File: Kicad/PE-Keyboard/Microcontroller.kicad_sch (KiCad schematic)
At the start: 34 parts, among them J1 USB_B_Micro, J2 Conn_01x02, J3 Conn_02x18_Odd_Even, J4 Conn_02x18_Odd_Even, U1 NCP1117-3.3_SOT223, U2 W25Q128JVS, U3 RP2040, Y1 ABLS-12.000MHZ-B4-T

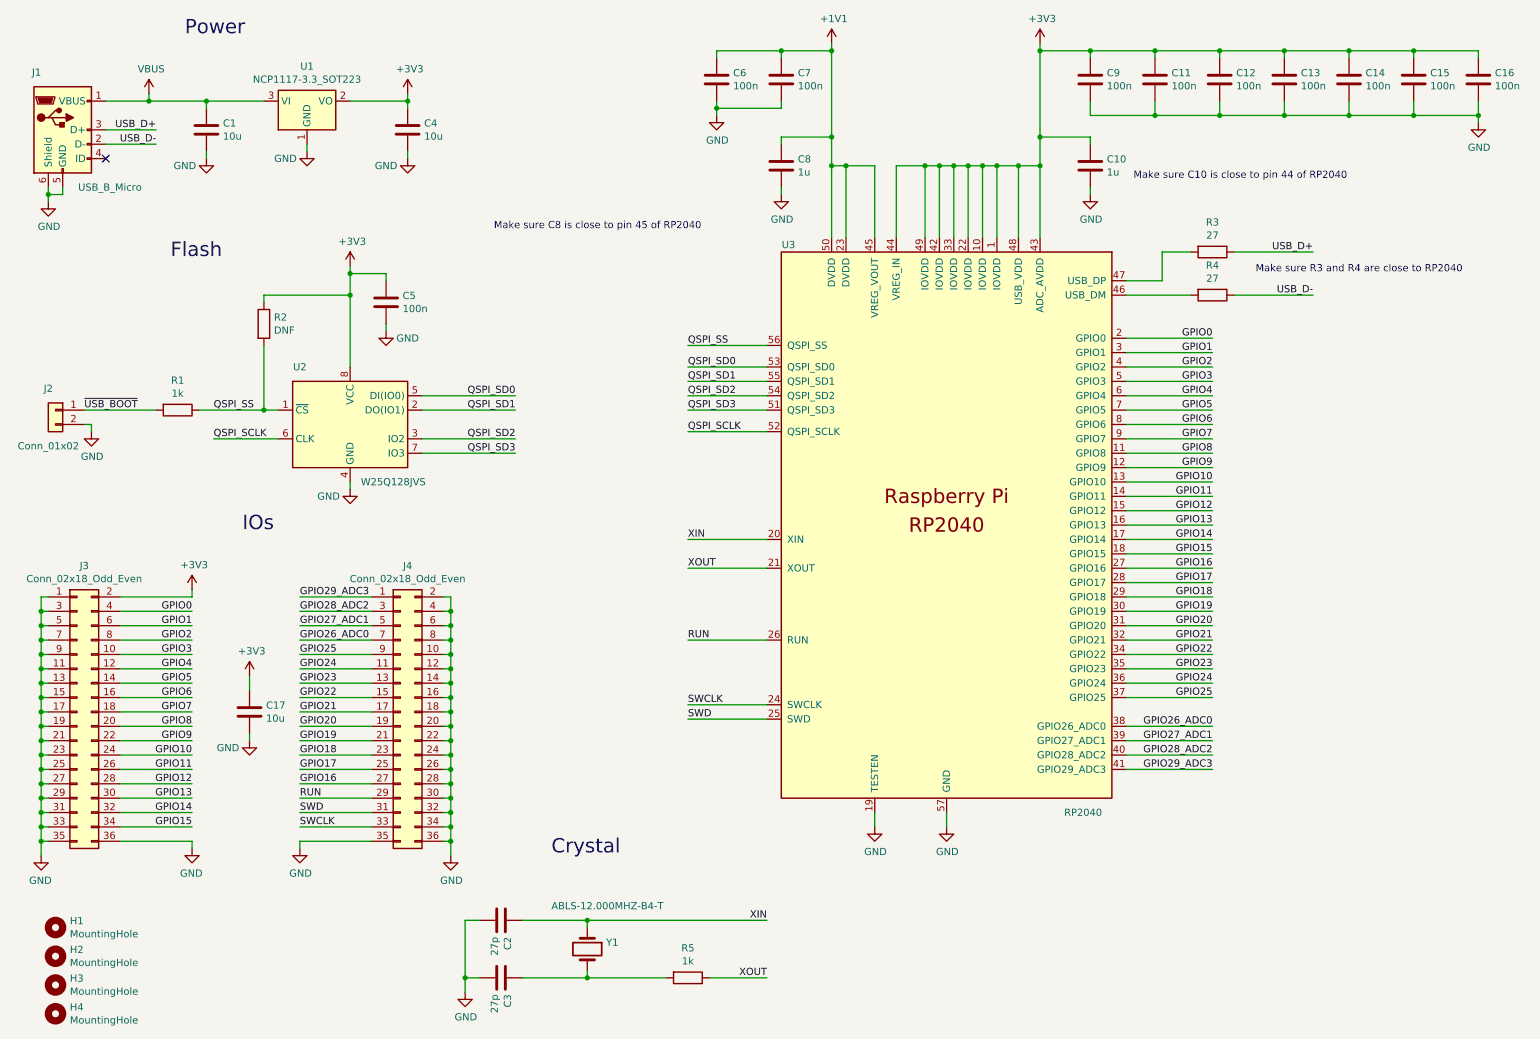
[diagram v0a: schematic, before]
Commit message: Started Sch and PCB
Laid out the buttons/Encoder. Chose a nice crystal, realized a connector in board gives challenges with routing.
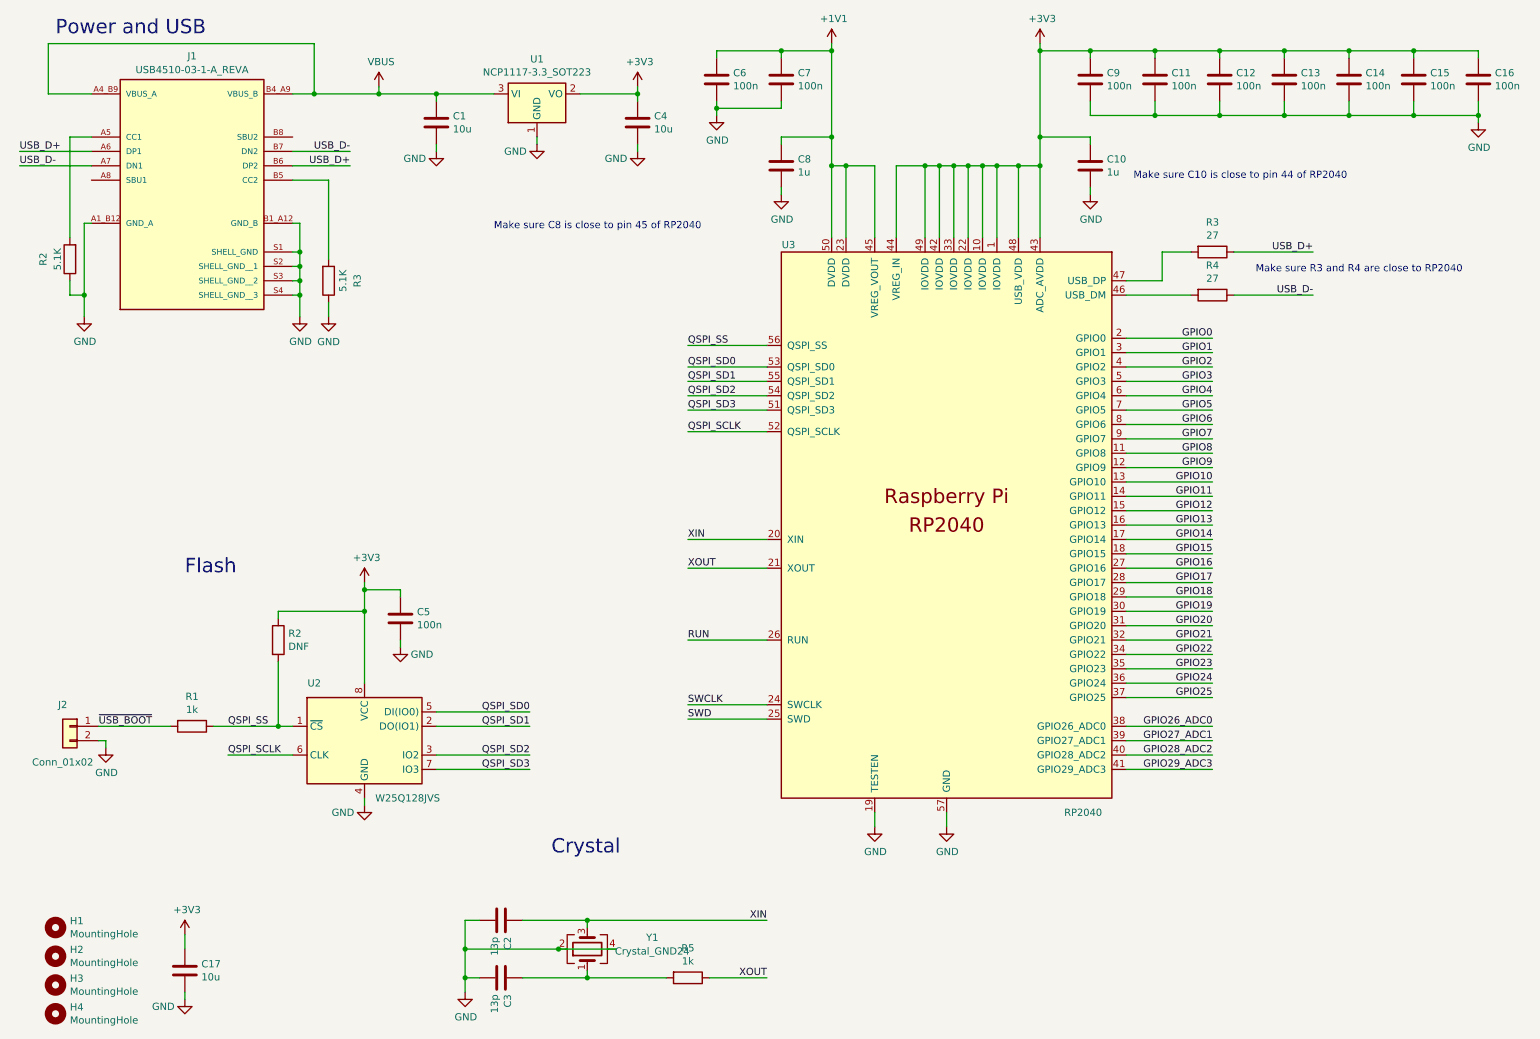
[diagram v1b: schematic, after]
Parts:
- removed J1: USB_B_Micro, RP2040:USB_Micro-B_Amphenol_10103594-0001LF_Horizontal_modified, symbol RP2040_minimal-rescue:USB_B_Micro-Connector
- removed J3, J4: Conn_02x18_Odd_Even, Connector_PinHeader_2.54mm:PinHeader_2x18_P2.54mm_Vertical, symbol Connector_Generic:Conn_02x18_Odd_Even
- removed Y1: ABLS-12.000MHZ-B4-T, RP2040:Crystal_SMD_HC49-US, symbol Device:Crystal
- added J1: USB4510-03-1-A_REVA, PE-Keyboard:GCT_USB4510-03-1-A_REVA, symbol USB4510-03-1-A_REVA:USB4510-03-1-A_REVA
- added R2, R3: 5.1K, Resistor_SMD:R_0603_1608Metric_Pad0.98x0.95mm_HandSolder, symbol Device:R
- added Y1: Crystal_GND24, Crystal:Crystal_SMD_0603-4Pin_6.0x3.5mm_HandSoldering, symbol Device:Crystal_GND24
- C10, C11, C12, C13, C14, C15, C16, C5, C6, C7, C8, C9: footprint Capacitor_SMD:C_0402_1005Metric -> Capacitor_SMD:C_0603_1608Metric_Pad1.08x0.95mm_HandSolder
- C2, C3: value 27p -> 13p; footprint Capacitor_SMD:C_0402_1005Metric -> Capacitor_SMD:C_0603_1608Metric_Pad1.08x0.95mm_HandSolder
- R1, R2, R3, R4, R5: footprint Capacitor_SMD:C_0402_1005Metric -> Resistor_SMD:R_0603_1608Metric_Pad0.98x0.95mm_HandSolder
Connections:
- net GND: now also J1.A1_B12 (GND_A), J1.B1_A12 (GND_B), J1.S1 (SHELL_GND), J1.S2 (SHELL_GND__1), J1.S3 (SHELL_GND__2), J1.S4 (SHELL_GND__3), R2.1, R3.1, Y1.2, Y1.4
- net USB_D+: now also J1.A6 (DP1), J1.B6 (DP2)
- net USB_D-: now also J1.A7 (DN1), J1.B7 (DN2)
- net VBUS: now also J1.A4_B9 (VBUS_A), J1.B4_A9 (VBUS_B)
- net XIN: now also Y1.3
- net at C3.1, R5.2: now also Y1.1
- new net: J1.A5 (CC1), R2.2
- new net: J1.B5 (CC2), R3.2
- no-connect marks 1 -> 0
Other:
- note added: "Power and USB"
- note removed: "IOs"
- note removed: "Power"
- moved on the sheet: C1, C17, C4, C5, J2, R1, R2, U1, U2
